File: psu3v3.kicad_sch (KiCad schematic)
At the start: 26 parts, among them U15 AP64501SP-13

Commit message: work on control logic
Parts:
- renumbered C34 to C36, C35 to C37, C36 to C38, C37 to C39, C38 to C40, C39 to C41, C40 to C42, C41 to C43, C42 to C44, C43 to C45, C44 to C46, C45 to C47, C46 to C48, C47 to C49, C48 to C50, C49 to C51, R56 to R59, R57 to R60, R58 to R61, R59 to R62, R60 to R63, U15 to U16
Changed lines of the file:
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@@
   (symbol (lib_id "Device:C_Small") (at 168.91 160.02 0) (unit 1)
     (in_bom yes) (on_board yes)
-    (property "Reference" "C41" (id 0) (at 171.45 158.75 0)
+    (property "Reference" "C43" (id 0) (at 171.45 158.75 0)
       (effects (font (size 1.27 1.27)) (justify left))
     )
@@
   (symbol (lib_id "Device:C_Small") (at 121.92 151.13 0) (unit 1)
     (in_bom yes) (on_board yes)
-    (property "Reference" "C37" (id 0) (at 124.46 149.86 0)
+    (property "Reference" "C39" (id 0) (at 124.46 149.86 0)
       (effects (font (size 1.27 1.27)) (justify left))
     )
@@
   (symbol (lib_id "power:GND") (at 152.4 171.45 0) (unit 1)
     (in_bom yes) (on_board yes)
-    (property "Reference" "#PWR043" (id 0) (at 152.4 177.8 0)
+    (property "Reference" "#PWR044" (id 0) (at 152.4 177.8 0)
       (effects (font (size 1.27 1.27)) hide)
     )
@@
   (symbol (lib_id "Capacitor_Tantalum_SMD_MyOwn:CP_EIA-7343-31_Kemet-D") (at 292.1 134.62 0) (unit 1)
     (in_bom yes) (on_board yes)
-    (property "Reference" "C49" (id 0) (at 294.64 133.35 0)
+    (property "Reference" "C51" (id 0) (at 294.64 133.35 0)
       (effects (font (size 1.27 1.27)) (justify left))
     )
@@
   (symbol (lib_id "Device:C_Small") (at 158.75 134.62 0) (unit 1)
     (in_bom yes) (on_board yes)
-    (property "Reference" "C40" (id 0) (at 161.29 133.35 0)
+    (property "Reference" "C42" (id 0) (at 161.29 133.35 0)
       (effects (font (size 1.27 1.27)) (justify left))
     )
@@
   (symbol (lib_id "Device:R_Small") (at 219.71 160.02 0) (unit 1)
     (in_bom yes) (on_board yes)
-    (property "Reference" "R59" (id 0) (at 220.98 158.75 0)
+    (property "Reference" "R62" (id 0) (at 220.98 158.75 0)
       (effects (font (size 1.27 1.27)) (justify left))
     )
@@
   (symbol (lib_id "Device:C_Small") (at 243.84 134.62 0) (unit 1)
     (in_bom yes) (on_board yes)
-    (property "Reference" "C45" (id 0) (at 246.38 133.35 0)
+    (property "Reference" "C47" (id 0) (at 246.38 133.35 0)
       (effects (font (size 1.27 1.27)) (justify left))
     )
@@
   (symbol (lib_id "Device:R_Small") (at 170.18 128.27 270) (unit 1)
     (in_bom yes) (on_board yes)
-    (property "Reference" "R56" (id 0) (at 168.91 125.73 90)
+    (property "Reference" "R59" (id 0) (at 168.91 125.73 90)
       (effects (font (size 1.27 1.27)) (justify left))
     )
@@
   (symbol (lib_id "Device:C_Small") (at 255.27 134.62 0) (unit 1)
     (in_bom yes) (on_board yes)
-    (property "Reference" "C46" (id 0) (at 257.81 133.35 0)
+    (property "Reference" "C48" (id 0) (at 257.81 133.35 0)
       (effects (font (size 1.27 1.27)) (justify left))
     )
@@
   (symbol (lib_id "Device:C_Small") (at 278.13 134.62 0) (unit 1)
     (in_bom yes) (on_board yes)
-    (property "Reference" "C48" (id 0) (at 280.67 133.35 0)
+    (property "Reference" "C50" (id 0) (at 280.67 133.35 0)
       (effects (font (size 1.27 1.27)) (justify left))
     )
@@
   (symbol (lib_id "Device:C_Small") (at 227.33 137.16 0) (unit 1)
     (in_bom no) (on_board no)
-    (property "Reference" "C44" (id 0) (at 229.87 135.89 0)
+    (property "Reference" "C46" (id 0) (at 229.87 135.89 0)
       (effects (font (size 1.27 1.27)) (justify left))
     )
@@
   (symbol (lib_id "power:GND") (at 292.1 171.45 0) (unit 1)
     (in_bom yes) (on_board yes)
-    (property "Reference" "#PWR047" (id 0) (at 292.1 177.8 0)
+    (property "Reference" "#PWR048" (id 0) (at 292.1 177.8 0)
       (effects (font (size 1.27 1.27)) hide)
     )
@@
   (symbol (lib_id "Device:R_Small") (at 307.975 134.62 0) (unit 1)
     (in_bom yes) (on_board yes)
-    (property "Reference" "R60" (id 0) (at 311.15 133.35 0))
+    (property "Reference" "R63" (id 0) (at 311.15 133.35 0))
     (property "Value" "1k" (id 1) (at 311.15 135.89 0))
     (property "Footprint" "Resistor_SMD:R_0402_1005Metric" (id 2) (at 307.975 134.62 0)
@@
   (symbol (lib_id "Device:R_Small") (at 208.28 156.21 0) (unit 1)
     (in_bom yes) (on_board yes)
-    (property "Reference" "R57" (id 0) (at 209.55 154.94 0)
+    (property "Reference" "R60" (id 0) (at 209.55 154.94 0)
       (effects (font (size 1.27 1.27)) (justify left))
     )
@@
   (symbol (lib_id "Device:C_Small") (at 91.44 151.13 0) (unit 1)
     (in_bom yes) (on_board yes)
-    (property "Reference" "C35" (id 0) (at 93.98 149.86 0)
+    (property "Reference" "C37" (id 0) (at 93.98 149.86 0)
       (effects (font (size 1.27 1.27)) (justify left))
     )
@@
   (symbol (lib_id "Device:C_Small") (at 208.28 163.83 0) (unit 1)
     (in_bom yes) (on_board yes)
-    (property "Reference" "C43" (id 0) (at 210.82 162.56 0)
+    (property "Reference" "C45" (id 0) (at 210.82 162.56 0)
       (effects (font (size 1.27 1.27)) (justify left))
     )
@@
   (symbol (lib_id "Device:C_Small") (at 76.2 151.13 0) (unit 1)
     (in_bom yes) (on_board yes)
-    (property "Reference" "C34" (id 0) (at 78.74 149.86 0)
+    (property "Reference" "C36" (id 0) (at 78.74 149.86 0)
       (effects (font (size 1.27 1.27)) (justify left))
     )
@@
   (symbol (lib_id "power:GND") (at 307.975 171.45 0) (unit 1)
     (in_bom yes) (on_board yes)
-    (property "Reference" "#PWR048" (id 0) (at 307.975 177.8 0)
+    (property "Reference" "#PWR049" (id 0) (at 307.975 177.8 0)
       (effects (font (size 1.27 1.27)) hide)
     )
@@
   (symbol (lib_id "Device:C_Small") (at 266.7 134.62 0) (unit 1)
     (in_bom yes) (on_board yes)
-    (property "Reference" "C47" (id 0) (at 269.24 133.35 0)
+    (property "Reference" "C49" (id 0) (at 269.24 133.35 0)
       (effects (font (size 1.27 1.27)) (justify left))
     )
@@
   (symbol (lib_id "Device:C_Small") (at 137.16 151.13 0) (unit 1)
     (in_bom yes) (on_board yes)
-    (property "Reference" "C38" (id 0) (at 139.7 149.86 0)
+    (property "Reference" "C40" (id 0) (at 139.7 149.86 0)
       (effects (font (size 1.27 1.27)) (justify left))
     )
@@
   (symbol (lib_id "power:GND") (at 278.13 171.45 0) (unit 1)
     (in_bom yes) (on_board yes)
-    (property "Reference" "#PWR046" (id 0) (at 278.13 177.8 0)
+    (property "Reference" "#PWR047" (id 0) (at 278.13 177.8 0)
       (effects (font (size 1.27 1.27)) hide)
     )
@@
   (symbol (lib_id "Device:R_Small") (at 212.09 137.16 0) (unit 1)
     (in_bom yes) (on_board yes)
-    (property "Reference" "R58" (id 0) (at 213.36 135.89 0)
+    (property "Reference" "R61" (id 0) (at 213.36 135.89 0)
       (effects (font (size 1.27 1.27)) (justify left))
     )
@@
   (symbol (lib_id "Regulator_Switching_Diodes:AP64501SP-13") (at 177.8 147.32 0) (unit 1)
     (in_bom yes) (on_board yes)
-    (property "Reference" "U15" (id 0) (at 177.165 137.16 0))
+    (property "Reference" "U16" (id 0) (at 177.165 137.16 0))
     (property "Value" "AP64501SP-13" (id 1) (at 177.8 139.7 0))
     (property "Footprint" "Regulator_Switching_Diodes:SOIC-8-1EP_3.9x4.9mm_P1.27mm_EP2.95x4.9mm_Mask2.71x3.4mm_ThermalVias" (id 2) (at 177.8 172.72 0)
@@
   (symbol (lib_id "Device:C_Small") (at 106.68 151.13 0) (unit 1)
     (in_bom yes) (on_board yes)
-    (property "Reference" "C36" (id 0) (at 109.22 149.86 0)
+    (property "Reference" "C38" (id 0) (at 109.22 149.86 0)
       (effects (font (size 1.27 1.27)) (justify left))
     )
@@
   (symbol (lib_id "power:GND") (at 251.46 171.45 0) (unit 1)
     (in_bom yes) (on_board yes)
-    (property "Reference" "#PWR045" (id 0) (at 251.46 177.8 0)
+    (property "Reference" "#PWR046" (id 0) (at 251.46 177.8 0)
       (effects (font (size 1.27 1.27)) hide)
     )
@@
   (symbol (lib_id "Device:C_Small") (at 196.85 160.02 0) (unit 1)
     (in_bom yes) (on_board yes)
-    (property "Reference" "C42" (id 0) (at 199.39 158.75 0)
+    (property "Reference" "C44" (id 0) (at 199.39 158.75 0)
       (effects (font (size 1.27 1.27)) (justify left))
     )
@@
   (symbol (lib_id "power:GND") (at 219.71 171.45 0) (unit 1)
     (in_bom yes) (on_board yes)
-    (property "Reference" "#PWR044" (id 0) (at 219.71 177.8 0)
+    (property "Reference" "#PWR045" (id 0) (at 219.71 177.8 0)
       (effects (font (size 1.27 1.27)) hide)
     )
@@
   (symbol (lib_id "Device:C_Small") (at 152.4 151.13 0) (unit 1)
     (in_bom yes) (on_board yes)
-    (property "Reference" "C39" (id 0) (at 154.94 149.86 0)
-      (effects (font (size 1.27 1.27)) (justify left))
-    )
+    (property "Reference" "C41" (id 0) (at 154.94 149.86 0)
+      (effects (font (size 1.27 1.27)) (justify left))
+    )

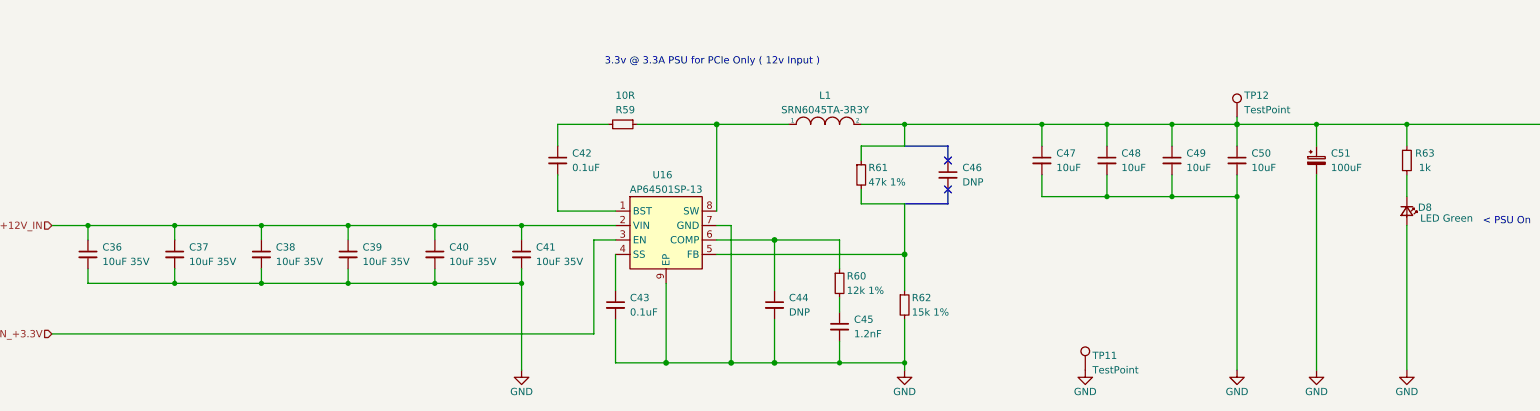
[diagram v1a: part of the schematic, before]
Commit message: connecterized faceplate, refreshed schematic
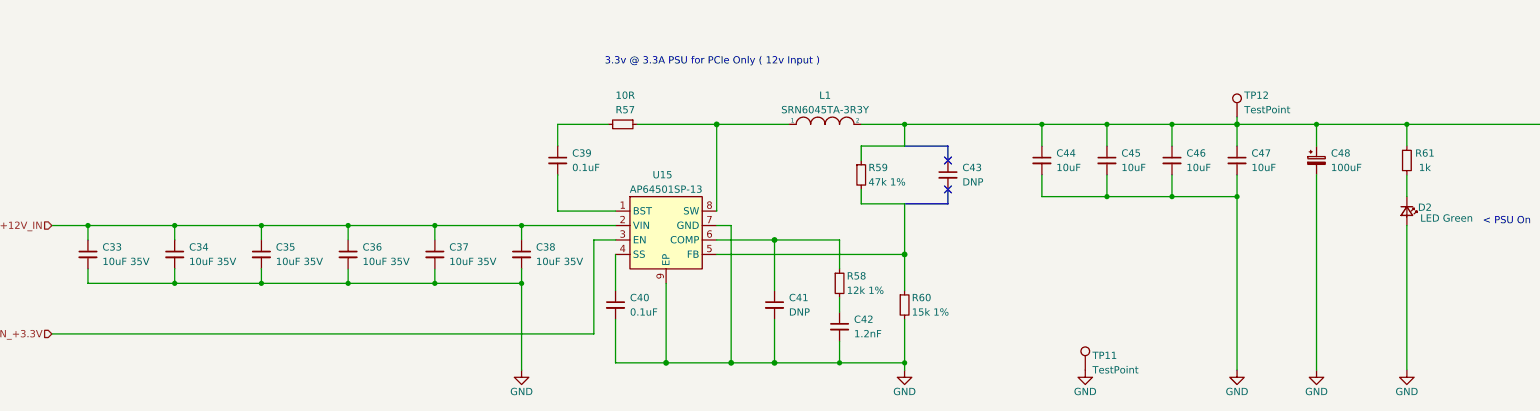
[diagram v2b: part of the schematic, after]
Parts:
- renumbered C36 to C33, C37 to C34, C38 to C35, C39 to C36, C40 to C37, C41 to C38, C42 to C39, C43 to C40, C44 to C41, C45 to C42, C46 to C43, C47 to C44, C48 to C45, C49 to C46, C50 to C47, C51 to C48, D8 to D2, R59 to R57, R60 to R58, R61 to R59, R62 to R60, R63 to R61, U16 to U15
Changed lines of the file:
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@@
   (symbol (lib_id "Device:C_Small") (at 168.91 160.02 0) (unit 1)
     (in_bom yes) (on_board yes)
-    (property "Reference" "C43" (id 0) (at 171.45 158.75 0)
+    (property "Reference" "C40" (id 0) (at 171.45 158.75 0)
       (effects (font (size 1.27 1.27)) (justify left))
     )
@@
   (symbol (lib_id "Device:C_Small") (at 121.92 151.13 0) (unit 1)
     (in_bom yes) (on_board yes)
-    (property "Reference" "C39" (id 0) (at 124.46 149.86 0)
+    (property "Reference" "C36" (id 0) (at 124.46 149.86 0)
       (effects (font (size 1.27 1.27)) (justify left))
     )
@@
   (symbol (lib_id "power:GND") (at 152.4 171.45 0) (unit 1)
     (in_bom yes) (on_board yes)
-    (property "Reference" "#PWR044" (id 0) (at 152.4 177.8 0)
+    (property "Reference" "#PWR043" (id 0) (at 152.4 177.8 0)
       (effects (font (size 1.27 1.27)) hide)
     )
@@
   (symbol (lib_id "Capacitor_Tantalum_SMD_MyOwn:CP_EIA-7343-31_Kemet-D") (at 292.1 134.62 0) (unit 1)
     (in_bom yes) (on_board yes)
-    (property "Reference" "C51" (id 0) (at 294.64 133.35 0)
+    (property "Reference" "C48" (id 0) (at 294.64 133.35 0)
       (effects (font (size 1.27 1.27)) (justify left))
     )
@@
   (symbol (lib_id "Device:C_Small") (at 158.75 134.62 0) (unit 1)
     (in_bom yes) (on_board yes)
-    (property "Reference" "C42" (id 0) (at 161.29 133.35 0)
+    (property "Reference" "C39" (id 0) (at 161.29 133.35 0)
       (effects (font (size 1.27 1.27)) (justify left))
     )
@@
   (symbol (lib_id "Device:R_Small") (at 219.71 160.02 0) (unit 1)
     (in_bom yes) (on_board yes)
-    (property "Reference" "R62" (id 0) (at 220.98 158.75 0)
+    (property "Reference" "R60" (id 0) (at 220.98 158.75 0)
       (effects (font (size 1.27 1.27)) (justify left))
     )
@@
   (symbol (lib_id "Device:C_Small") (at 243.84 134.62 0) (unit 1)
     (in_bom yes) (on_board yes)
-    (property "Reference" "C47" (id 0) (at 246.38 133.35 0)
+    (property "Reference" "C44" (id 0) (at 246.38 133.35 0)
       (effects (font (size 1.27 1.27)) (justify left))
     )
@@
   (symbol (lib_id "Device:R_Small") (at 170.18 128.27 270) (unit 1)
     (in_bom yes) (on_board yes)
-    (property "Reference" "R59" (id 0) (at 168.91 125.73 90)
+    (property "Reference" "R57" (id 0) (at 168.91 125.73 90)
       (effects (font (size 1.27 1.27)) (justify left))
     )
@@
   (symbol (lib_id "Device:C_Small") (at 255.27 134.62 0) (unit 1)
     (in_bom yes) (on_board yes)
-    (property "Reference" "C48" (id 0) (at 257.81 133.35 0)
+    (property "Reference" "C45" (id 0) (at 257.81 133.35 0)
       (effects (font (size 1.27 1.27)) (justify left))
     )
@@
   (symbol (lib_id "Device:C_Small") (at 278.13 134.62 0) (unit 1)
     (in_bom yes) (on_board yes)
-    (property "Reference" "C50" (id 0) (at 280.67 133.35 0)
+    (property "Reference" "C47" (id 0) (at 280.67 133.35 0)
       (effects (font (size 1.27 1.27)) (justify left))
     )
@@
   (symbol (lib_id "LED_SMD_LiteOn:LED Green") (at 307.975 143.51 270) (unit 1)
     (in_bom yes) (on_board yes)
-    (property "Reference" "D8" (id 0) (at 311.15 142.875 90))
+    (property "Reference" "D2" (id 0) (at 311.15 142.875 90))
     (property "Value" "LED Green" (id 1) (at 314.96 144.78 90))
     (property "Footprint" "LED_SMD_LiteOn:LED_0603_1608Metric_green" (id 2) (at 297.815 143.51 0)
@@
   (symbol (lib_id "Device:C_Small") (at 227.33 137.16 0) (unit 1)
     (in_bom no) (on_board no)
-    (property "Reference" "C46" (id 0) (at 229.87 135.89 0)
+    (property "Reference" "C43" (id 0) (at 229.87 135.89 0)
       (effects (font (size 1.27 1.27)) (justify left))
     )
@@
   (symbol (lib_id "power:GND") (at 292.1 171.45 0) (unit 1)
     (in_bom yes) (on_board yes)
-    (property "Reference" "#PWR048" (id 0) (at 292.1 177.8 0)
+    (property "Reference" "#PWR047" (id 0) (at 292.1 177.8 0)
       (effects (font (size 1.27 1.27)) hide)
     )
@@
   (symbol (lib_id "Device:R_Small") (at 307.975 134.62 0) (unit 1)
     (in_bom yes) (on_board yes)
-    (property "Reference" "R63" (id 0) (at 311.15 133.35 0))
+    (property "Reference" "R61" (id 0) (at 311.15 133.35 0))
     (property "Value" "1k" (id 1) (at 311.15 135.89 0))
     (property "Footprint" "Resistor_SMD:R_0402_1005Metric" (id 2) (at 307.975 134.62 0)
@@
   (symbol (lib_id "Device:R_Small") (at 208.28 156.21 0) (unit 1)
     (in_bom yes) (on_board yes)
-    (property "Reference" "R60" (id 0) (at 209.55 154.94 0)
+    (property "Reference" "R58" (id 0) (at 209.55 154.94 0)
       (effects (font (size 1.27 1.27)) (justify left))
     )
@@
   (symbol (lib_id "Device:C_Small") (at 91.44 151.13 0) (unit 1)
     (in_bom yes) (on_board yes)
-    (property "Reference" "C37" (id 0) (at 93.98 149.86 0)
+    (property "Reference" "C34" (id 0) (at 93.98 149.86 0)
       (effects (font (size 1.27 1.27)) (justify left))
     )
@@
   (symbol (lib_id "Device:C_Small") (at 208.28 163.83 0) (unit 1)
     (in_bom yes) (on_board yes)
-    (property "Reference" "C45" (id 0) (at 210.82 162.56 0)
+    (property "Reference" "C42" (id 0) (at 210.82 162.56 0)
       (effects (font (size 1.27 1.27)) (justify left))
     )
@@
   (symbol (lib_id "Device:C_Small") (at 76.2 151.13 0) (unit 1)
     (in_bom yes) (on_board yes)
-    (property "Reference" "C36" (id 0) (at 78.74 149.86 0)
+    (property "Reference" "C33" (id 0) (at 78.74 149.86 0)
       (effects (font (size 1.27 1.27)) (justify left))
     )
@@
   (symbol (lib_id "power:GND") (at 307.975 171.45 0) (unit 1)
     (in_bom yes) (on_board yes)
-    (property "Reference" "#PWR049" (id 0) (at 307.975 177.8 0)
+    (property "Reference" "#PWR048" (id 0) (at 307.975 177.8 0)
       (effects (font (size 1.27 1.27)) hide)
     )
@@
   (symbol (lib_id "Device:C_Small") (at 266.7 134.62 0) (unit 1)
     (in_bom yes) (on_board yes)
-    (property "Reference" "C49" (id 0) (at 269.24 133.35 0)
+    (property "Reference" "C46" (id 0) (at 269.24 133.35 0)
       (effects (font (size 1.27 1.27)) (justify left))
     )
@@
   (symbol (lib_id "Device:C_Small") (at 137.16 151.13 0) (unit 1)
     (in_bom yes) (on_board yes)
-    (property "Reference" "C40" (id 0) (at 139.7 149.86 0)
+    (property "Reference" "C37" (id 0) (at 139.7 149.86 0)
       (effects (font (size 1.27 1.27)) (justify left))
     )
@@
   (symbol (lib_id "power:GND") (at 278.13 171.45 0) (unit 1)
     (in_bom yes) (on_board yes)
-    (property "Reference" "#PWR047" (id 0) (at 278.13 177.8 0)
+    (property "Reference" "#PWR046" (id 0) (at 278.13 177.8 0)
       (effects (font (size 1.27 1.27)) hide)
     )
@@
   (symbol (lib_id "Device:R_Small") (at 212.09 137.16 0) (unit 1)
     (in_bom yes) (on_board yes)
-    (property "Reference" "R61" (id 0) (at 213.36 135.89 0)
+    (property "Reference" "R59" (id 0) (at 213.36 135.89 0)
       (effects (font (size 1.27 1.27)) (justify left))
     )
@@
   (symbol (lib_id "Regulator_Switching_Diodes:AP64501SP-13") (at 177.8 147.32 0) (unit 1)
     (in_bom yes) (on_board yes)
-    (property "Reference" "U16" (id 0) (at 177.165 137.16 0))
+    (property "Reference" "U15" (id 0) (at 177.165 137.16 0))
     (property "Value" "AP64501SP-13" (id 1) (at 177.8 139.7 0))
     (property "Footprint" "Regulator_Switching_Diodes:SOIC-8-1EP_3.9x4.9mm_P1.27mm_EP2.95x4.9mm_Mask2.71x3.4mm_ThermalVias" (id 2) (at 177.8 172.72 0)
@@
   (symbol (lib_id "Device:C_Small") (at 106.68 151.13 0) (unit 1)
     (in_bom yes) (on_board yes)
-    (property "Reference" "C38" (id 0) (at 109.22 149.86 0)
+    (property "Reference" "C35" (id 0) (at 109.22 149.86 0)
       (effects (font (size 1.27 1.27)) (justify left))
     )
@@
   (symbol (lib_id "power:GND") (at 251.46 171.45 0) (unit 1)
     (in_bom yes) (on_board yes)
-    (property "Reference" "#PWR046" (id 0) (at 251.46 177.8 0)
+    (property "Reference" "#PWR045" (id 0) (at 251.46 177.8 0)
       (effects (font (size 1.27 1.27)) hide)
     )
@@
   (symbol (lib_id "Device:C_Small") (at 196.85 160.02 0) (unit 1)
     (in_bom yes) (on_board yes)
-    (property "Reference" "C44" (id 0) (at 199.39 158.75 0)
+    (property "Reference" "C41" (id 0) (at 199.39 158.75 0)
       (effects (font (size 1.27 1.27)) (justify left))
     )
@@
   (symbol (lib_id "power:GND") (at 219.71 171.45 0) (unit 1)
     (in_bom yes) (on_board yes)
-    (property "Reference" "#PWR045" (id 0) (at 219.71 177.8 0)
+    (property "Reference" "#PWR044" (id 0) (at 219.71 177.8 0)
       (effects (font (size 1.27 1.27)) hide)
     )
@@
   (symbol (lib_id "Device:C_Small") (at 152.4 151.13 0) (unit 1)
     (in_bom yes) (on_board yes)
-    (property "Reference" "C41" (id 0) (at 154.94 149.86 0)
-      (effects (font (size 1.27 1.27)) (justify left))
-    )
+    (property "Reference" "C38" (id 0) (at 154.94 149.86 0)
+      (effects (font (size 1.27 1.27)) (justify left))
+    )
